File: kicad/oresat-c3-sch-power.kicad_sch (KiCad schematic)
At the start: 59 parts, among them U31 LP2985AIM5-3.3, U34 TPS259621DDA, U35 TPS259620DDA, U36 LTC3624-5, U38 LP2985AIM5-3.3, U6 LTC3624-5

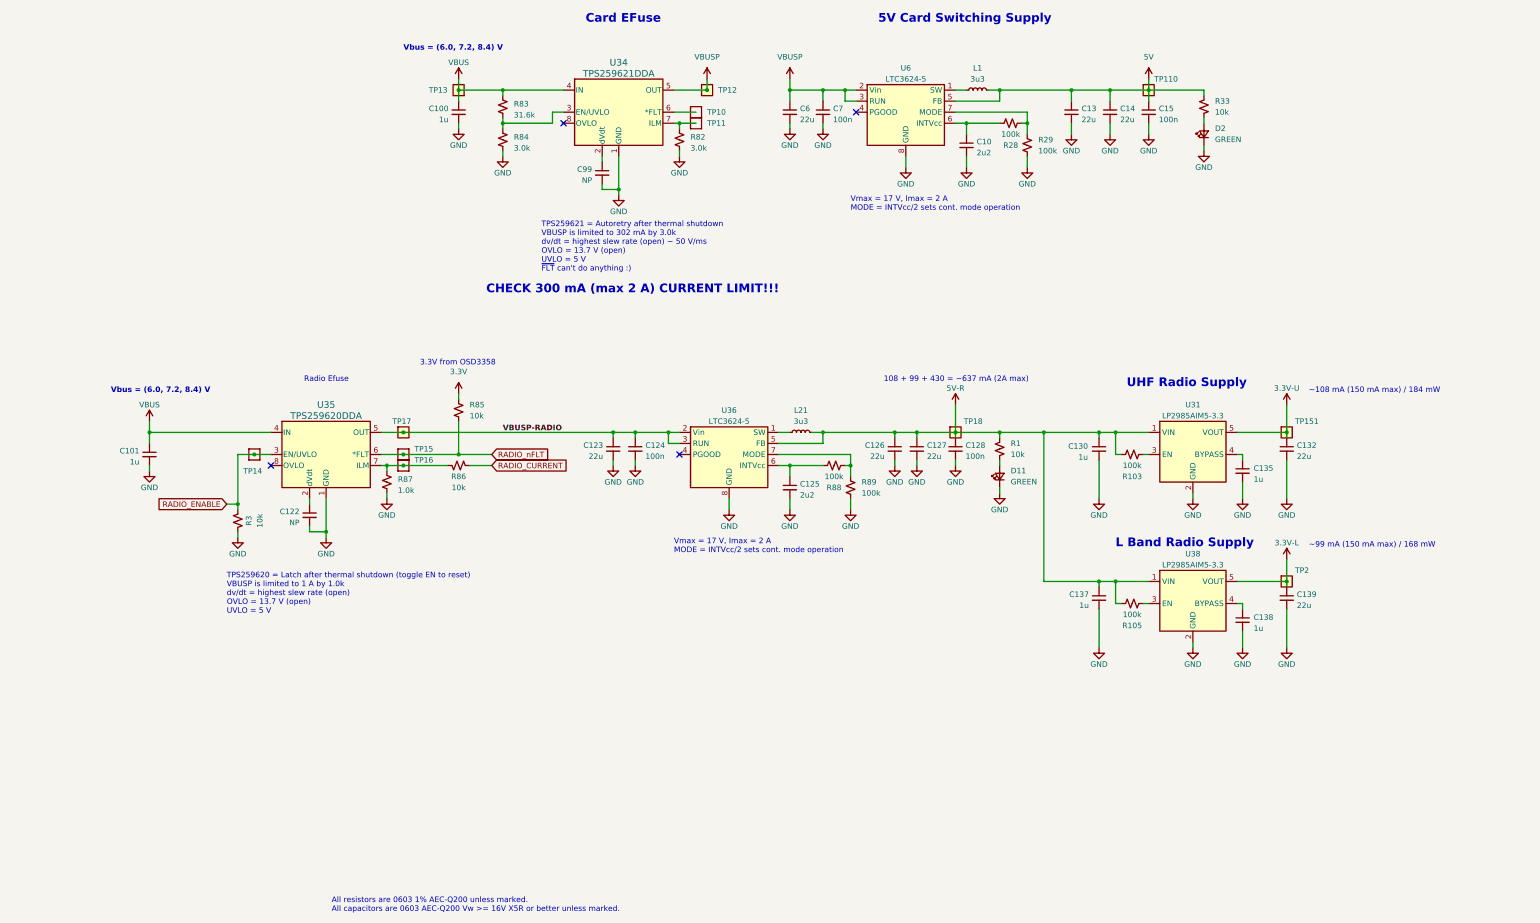
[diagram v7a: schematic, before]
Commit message: More polish; fixed all non-RF DRCs.
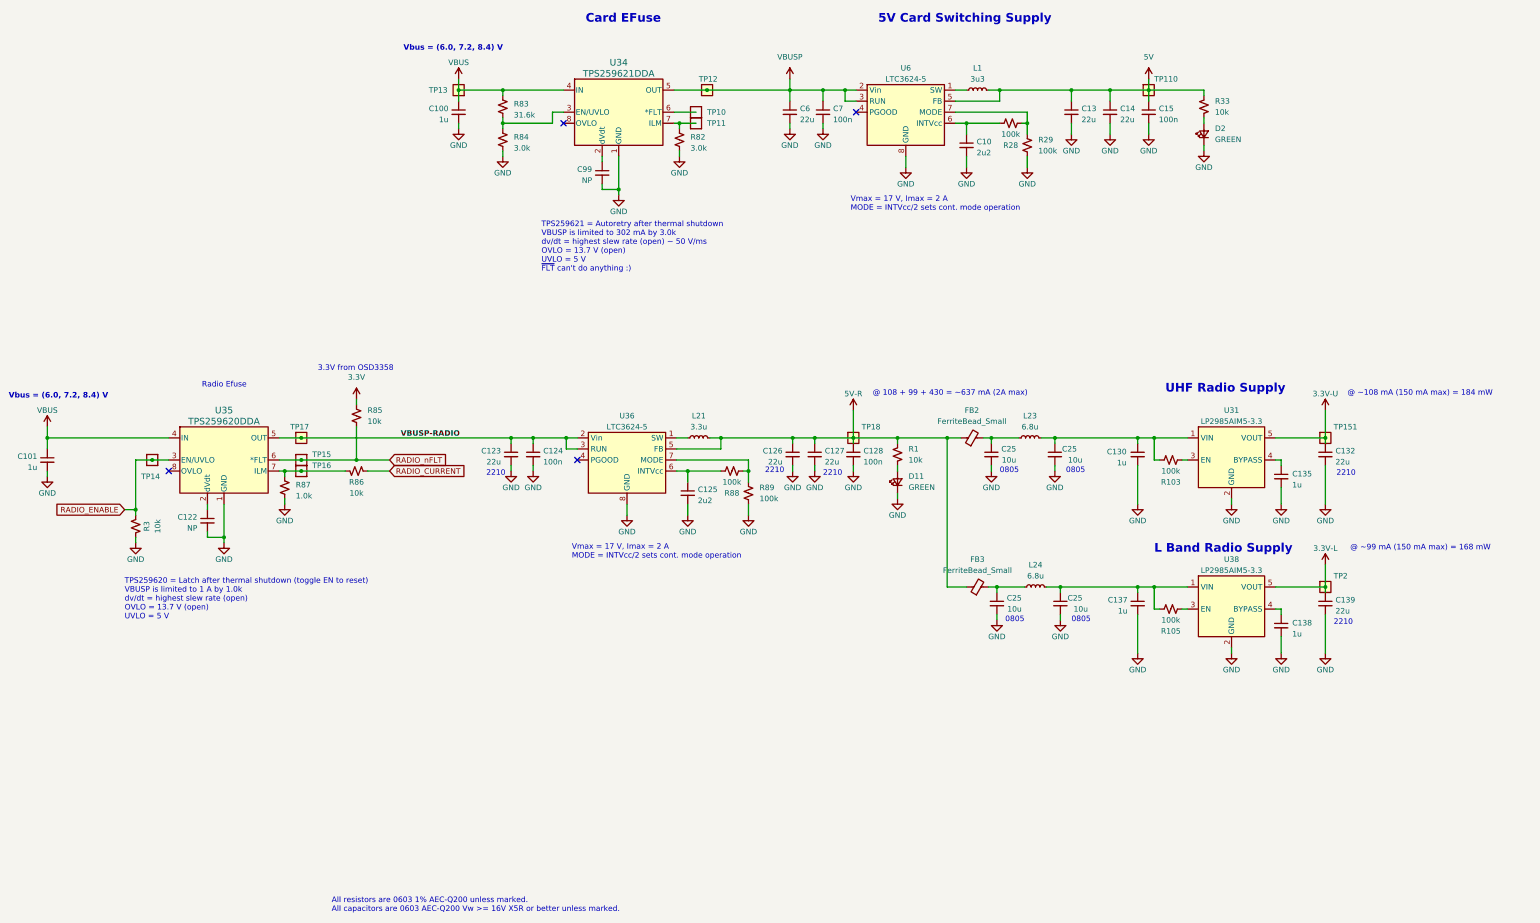
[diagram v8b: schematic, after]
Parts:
- added C25 (x4): 10u, Capacitor_SMD:C_0805_2012Metric, symbol Device:C_Small
- added FB2, FB3: FerriteBead_Small, Resistor_SMD:R_0805_2012Metric, symbol Device:FerriteBead_Small
- added L23, L24: 6.8u, oresat-passives:L_ECS-MPI4040, symbol Device:L_Small
- L21: value 3u3 -> 3.3u
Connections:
- net 5V-R: now also FB2.1, FB3.1; no longer C130.1, C137.1, R103.1, R105.1, U31.1 (VIN), U38.1 (VIN)
- net GND: now also C25.2, C25.2, C25.2, C25.2
- new net: C130.1, C25.1, L23.2, R103.1, U31.1 (VIN)
- new net: C25.1, FB2.2, L23.1
- new net: C137.1, C25.1, L24.2, R105.1, U38.1 (VIN)
- new net: C25.1, FB3.2, L24.1
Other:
- note added: "0805"
- note added: "2210"
- note added: "@ 108 + 99 + 430 = ~637 mA (2A max)"
- note added: "@ ~108 mA (150 mA max) = 184 mW"
- note added: "@ ~99 mA (150 mA max) = 168 mW"
- note removed: "108 + 99 + 430 = ~637 mA (2A max)"
- note removed: "CHECK 300 mA (max 2 A) CURRENT LIMIT!!!"
- note removed: "~108 mA (150 mA max) / 184 mW"
- note removed: "~99 mA (150 mA max) / 168 mW"
- moved on the sheet: C101, C122, C123, C124, C125, C126, C127, C128, C130, C132, C135, C137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
